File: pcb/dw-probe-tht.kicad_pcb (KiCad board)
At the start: 2 copper layers, 68.6 x 53.3 mm, 26 parts, among them Q1 IRLML6402, Q2 IRLML6402, SW1 SW_Push, U1 LM1117T-3.3

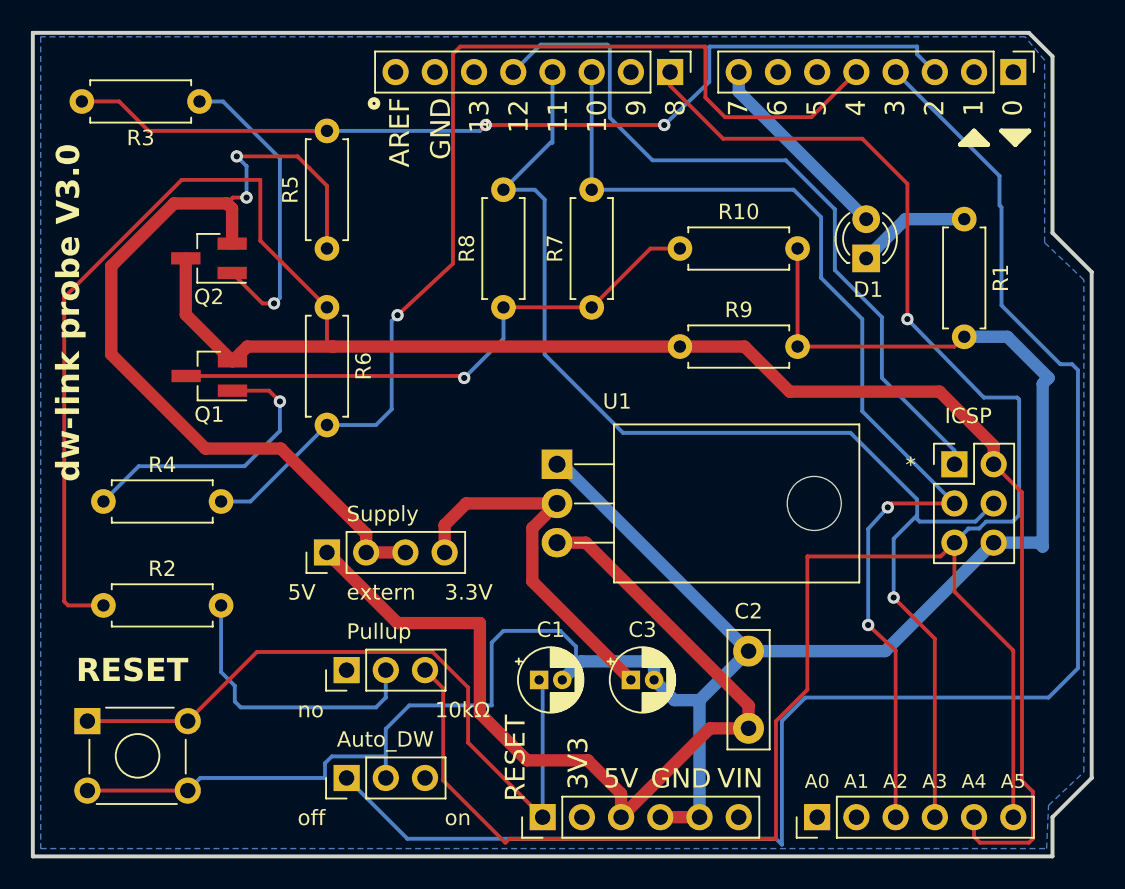
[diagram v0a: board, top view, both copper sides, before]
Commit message: new dw-link probe V3.1
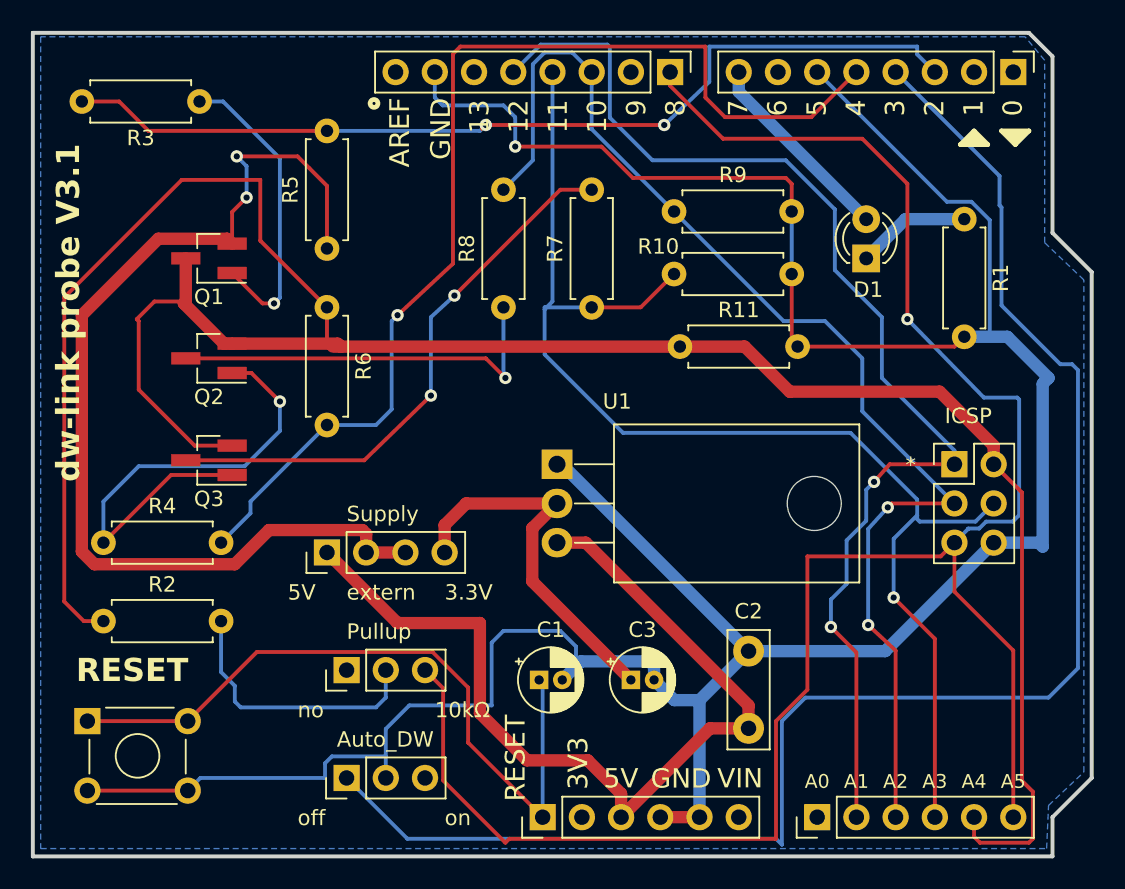
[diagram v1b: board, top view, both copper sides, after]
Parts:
- added Q3: IRLML6402, Package_TO_SOT_SMD:SOT-23_Handsoldering, F.Cu at (107.9, 96.3)
- added R9: 10MΩ, Resistor_THT:R_Axial_DIN0207_L6.3mm_D2.5mm_P7.62mm_Horizontal, F.Cu at (138.0, 80.2)
- moved R4 2.67 mm to (101.1, 101.6)
- moved R10 1.69 mm to (138.0, 84.2)
- moved Q2 1.14 mm to (107.9, 89.7)
- moved R2 1.02 mm to (101.1, 106.7)
- renumbered Q2 to Q1, Q1 to Q2, R9 to R11
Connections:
- AD1 pad 2: unconnected-(AD1-Pad2) -> Net-(AD1-Pad2)
- IOH1 pad 5: Net-(IOH1-Pad5) -> Net-(AD1-Pad2)
- IOL1 pad 6: unconnected-(IOL1-Pad6) -> GND
- JP1 pad 1: Net-(IOH1-Pad5) -> Net-(AD1-Pad2)
- Q2 pad 3: Net-(Q1-D) -> Net-(Q2-D)
- R10 pad 1: Net-(Q1-D) -> Net-(AD1-Pad4)
- R7 pad 1: Net-(Q1-D) -> Net-(AD1-Pad4)
- R7 pad 2: Net-(AD1-Pad3) -> Net-(Q3-D)
- R8 pad 1: Net-(Q1-D) -> Net-(Q2-D)
- R8 pad 2: Net-(AD1-Pad4) -> Net-(AD1-Pad3)
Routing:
- net Net-(AD1-Pad2): track 0.00 -> 77.9 mm, vias 0 -> 2
- net GND: track 143.1 -> 198.5 mm, vias 0 -> 1
- net Net-(IOH1-Pad5): track 48.4 -> 0.00 mm
- net Net-(Q1-D): track 37.0 -> 0.00 mm, vias 1 -> 0
- net Net-(Q3-D): track 0.00 -> 36.9 mm, vias 0 -> 2
- net Net-(Q2-D): track 0.00 -> 25.9 mm, vias 0 -> 1
- net VCC: track 143.5 -> 159.2 mm
- net Net-(Q2-G): track 18.8 -> 32.2 mm
- net Net-(Q1-S): track 57.9 -> 67.9 mm
- net Net-(AD1-Pad3): track 71.5 -> 79.0 mm
- net Net-(AD1-Pad4): track 78.1 -> 84.0 mm
- net Net-(IOL1-Pad5): track 69.9 -> 71.4 mm
- net Net-(Pullup1-Pin_2): track 18.6 -> 17.6 mm
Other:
- board text added: "dw-link probe V3.1"
- board text removed: "dw-link probe V3.0"
